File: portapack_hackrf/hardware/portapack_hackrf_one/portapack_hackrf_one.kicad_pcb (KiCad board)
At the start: 4 copper layers, 120 x 75 mm, 92 parts, among them J2 MICROSD_DETSW, J3 KINGTECH_DW0240A2BZ_FPC, P1 TRRS_SW_JACK, P2 TRS_JACK, P20 HACKRF_ONE_P20, P22 HACKRF_ONE_P22, P28 HACKRF_ONE_P28, P3 TRS_JACK, Q1 MOSFET_P, Q2 MOSFET_P, Q3 MOSFET_N, SW1 CK_TSWB-3N-CB, U1 5M40ZE64, U2 REGULATOR_SOT23_5, U3 WM8731SEDS, X1 MIC_ELECTRET

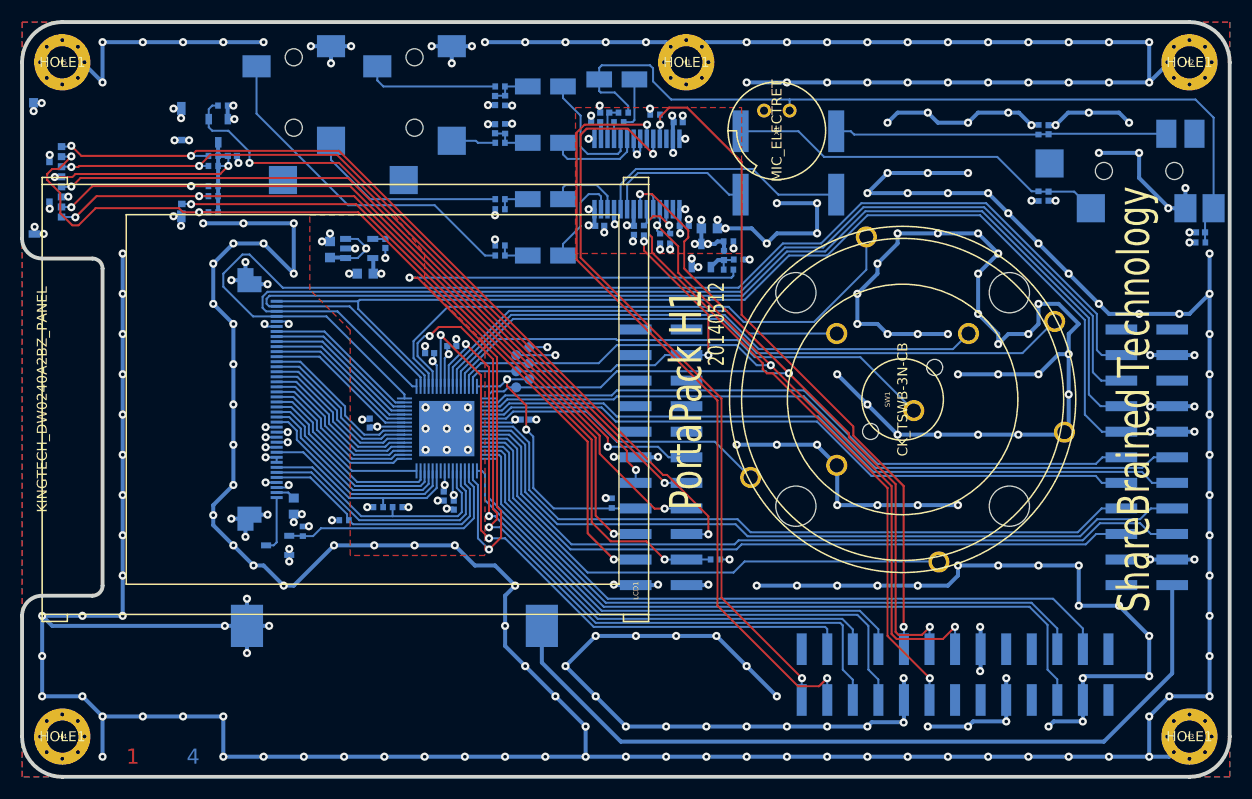
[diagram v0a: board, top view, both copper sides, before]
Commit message: Major revision 20140701 of PortaPack H1 PCB design for second prototype. Slight changes to signal mapping to CPLD. Added lots of signal integrity and EMC tweaks, including series resistor terminations and ferrites on audio jacks. Removed a bunch of unnecessary components. Shifted LCD to 1.8V I/O operation. Added more bypass capacitors.
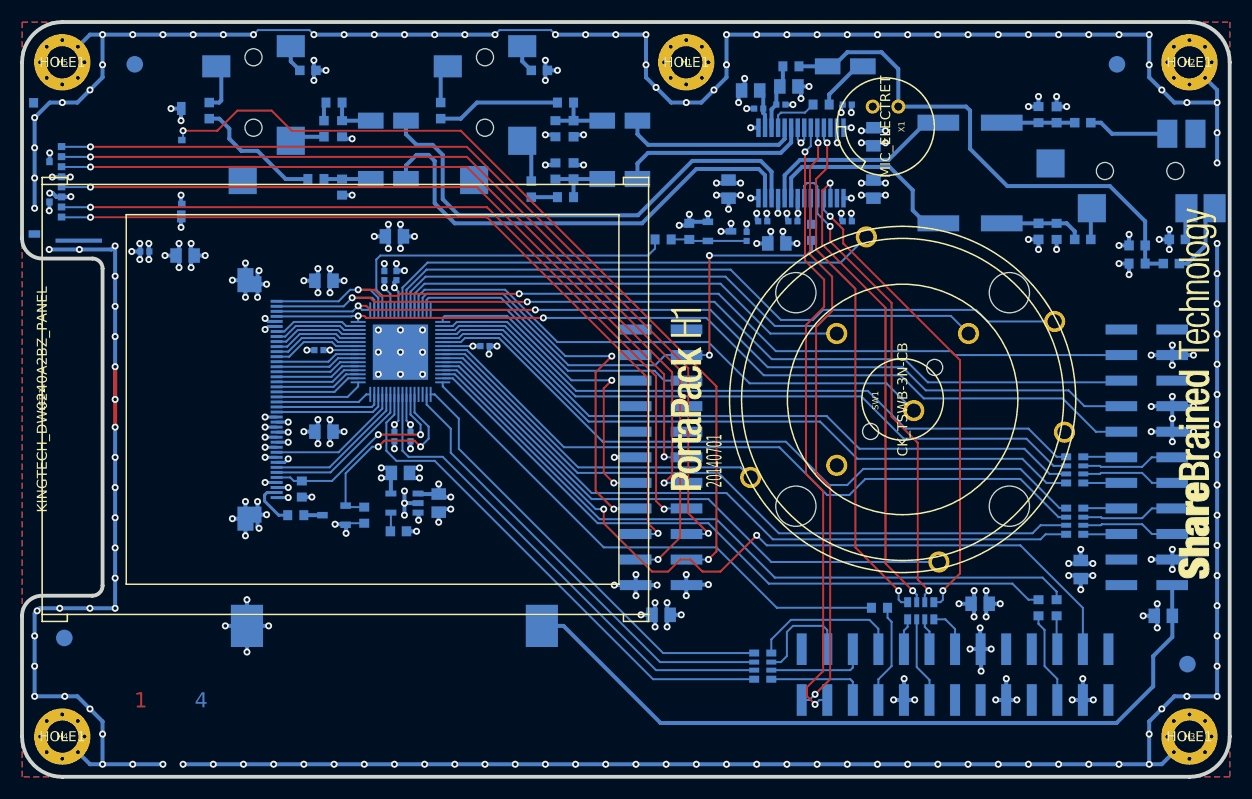
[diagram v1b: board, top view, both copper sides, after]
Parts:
- removed Q3: MOSFET_N, ipc_sot:IPC_SOT95P230X110-3N
- removed R23, R24, R25, R27, R28, R29, R31, R32, R33: 10K, ipc_resc:IPC_RESC1005X40N
- removed R26: 100R, ipc_resc:IPC_RESC1005X40N
- removed R30: R, ipc_resc:IPC_RESC1608X55N
- removed TP1, TP2, TP3, TP4, TP5, TP6: TP, tp:TP_1MM
- added C31: 100N, ipc_capc:IPC_CAPC1005X55N, B.Cu at (98.6, 141.2)
- added C32: 10U, ipc_capc:IPC_CAPC2012X140N, B.Cu at (123.5, 158.9)
- added C33: 100N, ipc_capc:IPC_CAPC1005X55N, B.Cu at (97.0, 141.2)
- added C34: 10U, ipc_capc:IPC_CAPC2012X140N, B.Cu at (97.0, 121.3)
- added C35: 100N, ipc_capc:IPC_CAPC1005X55N, B.Cu at (89.5, 132.6)
- added C36: 10U, ipc_capc:IPC_CAPC2012X140N, B.Cu at (90.0, 125.7)
- added C37: 10U, ipc_capc:IPC_CAPC2012X140N, B.Cu at (90.0, 140.7)
- added C38: 10U, ipc_capc:IPC_CAPC2012X140N, B.Cu at (101.4, 147.8)
- added C39: DNI, ipc_capc:IPC_CAPC1608X90N, B.Cu at (97.4, 150.6)
- added C40: 10U, ipc_capc:IPC_CAPC2012X140N, B.Cu at (97.6, 144.8)
- added C41: 10U, ipc_capc:IPC_CAPC2012X140N, B.Cu at (173.4, 159.0)
- added C42: 10U, ipc_capc:IPC_CAPC2012X140N, B.Cu at (155.2, 157.8)
- added C43: 10U, ipc_capc:IPC_CAPC2012X140N, B.Cu at (165.2, 154.4)
- added FID1: FIDUCIAL, fiducial:FIDUCIAL_65MIL, B.Cu at (71.2, 104.2)
- added FID2: FIDUCIAL, fiducial:FIDUCIAL_65MIL, B.Cu at (168.8, 104.2)
- added FID3: FIDUCIAL, fiducial:FIDUCIAL_65MIL, B.Cu at (64.2, 161.2)
- added FID4: FIDUCIAL, fiducial:FIDUCIAL_65MIL, B.Cu at (175.8, 163.8)
- added L1: L, ipc_indc:IPC_INDC1608X95N, B.Cu at (111.4, 104.8)
- added L10: L, ipc_indc:IPC_INDC1608X95N, B.Cu at (88.4, 104.8)
- added L2: L, ipc_indc:IPC_INDC1608X95N, B.Cu at (110.6, 116.6)
- added L3: L, ipc_indc:IPC_INDC1608X95N, B.Cu at (101.6, 108.8)
- added L4: L, ipc_indc:IPC_INDC1608X95N, B.Cu at (165.4, 121.6)
- added L5: L, ipc_indc:IPC_INDC1608X95N, B.Cu at (165.4, 110.0)
- added L6: L, ipc_indc:IPC_INDC1608X95N, B.Cu at (174.8, 121.6)
- added L7: L, ipc_indc:IPC_INDC1608X95N, B.Cu at (90.0, 110.6)
- added L8: L, ipc_indc:IPC_INDC1608X95N, B.Cu at (78.6, 108.8)
- added L9: L, ipc_indc:IPC_INDC1608X95N, B.Cu at (174.2, 124.0)
- added LOGO1: SHAREBRAINED, sharebrained:sharebrained_text_300, F.Cu at (176.7, 137.0)
- added LOGO2: PORTAPACK_H1, sharebrained:portapack_text_300, F.Cu at (126.0, 137.5)
- added RP1: 100R, ipc_resc:IPC_RESCAXS80P160X320X60-8N, B.Cu at (149.3, 158.5)
- added RP4: 100R, ipc_resc:IPC_RESCAXS80P160X320X60-8N, B.Cu at (133.6, 164.0)
- added RP6: 100R, ipc_resc:IPC_RESCAXS80P160X320X60-8N, B.Cu at (164.6, 144.5)
- added RP7: 100R, ipc_resc:IPC_RESCAXS80P160X320X60-8N, B.Cu at (164.6, 149.6)
- C1, C2: value 220U -> 100N; footprint ipc_capae:IPC_CAPAE830X620N -> ipc_capc:IPC_CAPC1005X55N
- C10, C4, C5, C6: value 220P -> 100N
- C11, C12: value 1U -> 10U; footprint ipc_capae:IPC_CAPAE430X540N -> ipc_capc:IPC_CAPC2012X140N
- C13: footprint ipc_capae:IPC_CAPAE430X540N -> ipc_capc:IPC_CAPC2012X140N
- C14: value 10U -> 220P; footprint ipc_capae:IPC_CAPAE430X540N -> ipc_capc:IPC_CAPC1608X95N
- C15, C22, C25: value 100N -> 220P; footprint ipc_capc:IPC_CAPC1005X55N -> ipc_capc:IPC_CAPC1608X95N
- C16, C24: value 100N -> 1U; footprint ipc_capc:IPC_CAPC1005X55N -> ipc_capae:IPC_CAPAE430X540N
- C17: footprint ipc_capc:IPC_CAPC1608X95N -> ipc_capae:IPC_CAPAE430X540N
- C18, C19: value 100N -> 220U; footprint ipc_capc:IPC_CAPC1005X55N -> ipc_capae:IPC_CAPAE830X620N
- C20, C21: value 100N -> 10U; footprint ipc_capc:IPC_CAPC1005X55N -> ipc_capae:IPC_CAPAE430X540N
- C23: value DNI -> 220P; footprint ipc_capc:IPC_CAPC1005X55N -> ipc_capc:IPC_CAPC1608X95N
- C26, C7: value 100N -> 10U; footprint ipc_capc:IPC_CAPC1005X55N -> ipc_capc:IPC_CAPC2012X140N
- C27: value 10U -> 100N; footprint ipc_capc:IPC_CAPC1608X95N -> ipc_capc:IPC_CAPC1005X55N
- C3: value 1U -> 100N; footprint ipc_capae:IPC_CAPAE430X540N -> ipc_capc:IPC_CAPC1005X55N
- C8: footprint ipc_capc:IPC_CAPC1608X95N -> ipc_capc:IPC_CAPC2012X140N
- C9: value 220P -> 10U; footprint ipc_capc:IPC_CAPC1005X55N -> ipc_capc:IPC_CAPC2012X140N
- P1: value TRRS_SW_JACK -> TRS_JACK; footprint cui:CUI_SJ-43516-SMT -> cui:CUI_SJ-3524-SMT
- P2: value TRS_JACK -> TRRS_SW_JACK; footprint cui:CUI_SJ-3524-SMT -> cui:CUI_SJ-43516-SMT
- R1: value R -> 100R; footprint ipc_resc:IPC_RESC1005X40N -> ipc_resc:IPC_RESC1608X55N
- R10: value 5K6 -> R; footprint ipc_resc:IPC_RESC1005X40N -> ipc_resc:IPC_RESC1608X55N
- R11: value 5K6 -> 47K; footprint ipc_resc:IPC_RESC1005X40N -> ipc_resc:IPC_RESC1608X55N
- R12, R13, R14: value 10K -> 47K; footprint ipc_resc:IPC_RESC1005X40N -> ipc_resc:IPC_RESC1608X55N
- R15, R16: value 10K -> 100R; footprint ipc_resc:IPC_RESC1005X40N -> ipc_resc:IPC_RESC1608X55N
- R17, R19, R20, R22, R7, R8: footprint ipc_resc:IPC_RESC1005X40N -> ipc_resc:IPC_RESC1608X55N
- R18: value 47K -> 680R; footprint ipc_resc:IPC_RESC1005X40N -> ipc_resc:IPC_RESC1608X55N
- R2, R3: value 47K -> 100R; footprint ipc_resc:IPC_RESC1005X40N -> ipc_resc:IPC_RESC1608X55N
- R21: value 100R -> R; footprint ipc_resc:IPC_RESC1005X40N -> ipc_resc:IPC_RESC1608X55N
- R4: value 47K -> 10K; footprint ipc_resc:IPC_RESC1005X40N -> ipc_resc:IPC_RESC1608X55N
- R5: value 680R -> 47K; footprint ipc_resc:IPC_RESC1005X40N -> ipc_resc:IPC_RESC1608X55N
- R6: value 10K -> 5K6; footprint ipc_resc:IPC_RESC1005X40N -> ipc_resc:IPC_RESC1608X55N
- R9: value 100K -> 5K6; footprint ipc_resc:IPC_RESC1005X40N -> ipc_resc:IPC_RESC1608X55N
- U1: value 5M40ZE64 -> WM8731SEDS; footprint ipc_qfp:IPC_QFP40P900X900X120-65N -> ipc_sop:IPC_SOP65P780X200-28N
- U3: value WM8731SEDS -> 5M40ZE64; footprint ipc_sop:IPC_SOP65P780X200-28N -> ipc_qfp:IPC_QFP40P900X900X120-65N
- moved P2 73.6 mm to (172.1, 114.8), turned to 180 degrees
- moved P1 73.5 mm to (106.0, 106.0), turned to 270 degrees
- moved C23 67.9 mm to (162.8, 109.2), turned to 90 degrees
- moved R1 65.0 mm to (162.8, 158.2), turned to 270 degrees
- moved R17 63.5 mm to (170.8, 124.0), turned to 180 degrees
- moved C22 59.4 mm to (161.0, 120.8), turned to 90 degrees
- moved R13 56.6 mm to (91.8, 110.6), turned to 90 degrees
- moved R11 56.3 mm to (162.8, 120.8), turned to 90 degrees
- moved C25 53.4 mm to (170.8, 122.2), turned to 180 degrees
- moved R4 53.4 mm to (123.7, 121.6)
- moved R3 50.1 mm to (145.2, 158.2), turned to 0 degrees
- moved C18 48.3 mm to (154.2, 120.0)
- moved C6 45.6 mm to (133.2, 108.6)
- moved U1 44.0 mm to (137.4, 114.0), turned to 90 degrees
- moved R2 40.9 mm to (161.0, 158.2), turned to 270 degrees
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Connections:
- net /SD_CLK renamed /hackrf_if/SD_CLK
- net /VBAT renamed /hackrf_if/VBAT
- C1 pad 1: /LHPOUT -> /audio/CODEC_VDD
- C10 pad 1: Net-(C10-Pad1) -> /audio/MICBIAS
- C11 pad 1: /LLINEIN -> /audio/CODEC_VDD
- C11 pad 2: Net-(C11-Pad2) -> GND
- C12 pad 1: /RLINEIN -> /audio/MICBIAS
- C12 pad 2: Net-(C10-Pad1) -> GND
- C13 pad 1: /LOUT -> /audio/CODEC_VDD
- C13 pad 2: Net-(C13-Pad2) -> GND
- C14 pad 1: /ROUT -> GND
- C16 pad 1: +3.3V -> /audio/LLINEIN
- C16 pad 2: GND -> Net-(C14-Pad2)
- C17 pad 1: +3.3V -> /audio/RLINEIN
- C17 pad 2: GND -> Net-(C15-Pad1)
- C18 pad 1: +3.3V -> /audio/LHPOUT
- C18 pad 2: GND -> Net-(C18-Pad2)
- C19 pad 1: /CODEC_VDD -> /audio/RHPOUT
- C19 pad 2: GND -> Net-(C19-Pad2)
- C2 pad 1: /RHPOUT -> /audio/CODEC_VDD
- C2 pad 2: Net-(C2-Pad2) -> GND
- C20 pad 1: +3.3V -> /audio/LOUT
- C20 pad 2: GND -> Net-(C20-Pad2)
- C21 pad 1: +3.3V -> /audio/ROUT
- C21 pad 2: GND -> Net-(C21-Pad2)
- C22 pad 1: +1.8V -> GND
- C22 pad 2: GND -> Net-(C18-Pad2)
- C23 pad 1: Net-(C23-Pad1) -> Net-(C19-Pad2)
- C24 pad 1: GND -> Net-(C24-Pad1)
- C24 pad 2: /CODEC_VDD -> Net-(C24-Pad2)
- C25 pad 1: /CODEC_VDD -> Net-(C24-Pad2)
- C26 pad 1: +1.8V -> +3.3V
- C27 pad 1: +1.8V -> +3.3V
- C28 pad 1: GND -> +3.3V
- C28 pad 2: /CODEC_VDD -> GND
- C29 pad 1: Net-(C29-Pad1) -> +1.8V
- C3 pad 1: Net-(C3-Pad1) -> /audio/CODEC_VDD
- C3 pad 2: Net-(C3-Pad2) -> GND
- C30 pad 1: /MICBIAS -> +3.3V
- C4 pad 1: GND -> /audio/CODEC_VDD
- C4 pad 2: Net-(C1-Pad2) -> GND
- C5 pad 1: Net-(C2-Pad2) -> /audio/CODEC_VDD
- C6 pad 1: Net-(C3-Pad2) -> /audio/VMID
- C7 pad 1: /CODEC_VDD -> /audio/CODEC_VDD
- C7 pad 2: Net-(C7-Pad2) -> GND
- C8 pad 1: /CODEC_VDD -> /audio/VMID
- C9 pad 1: GND -> /audio/CODEC_VDD
- C9 pad 2: Net-(C11-Pad2) -> GND
- J2 pad 1: /SD_DAT2 -> /hackrf_if/SD_DAT2
- J2 pad 2: /SD_DAT3 -> /hackrf_if/SD_DAT3
- J2 pad 3: /SD_CMD -> /hackrf_if/SD_CMD
- J2 pad 4: Net-(C15-Pad1) -> +3.3V
- J2 pad 7: /SD_DAT0 -> /hackrf_if/SD_DAT0
- J2 pad 8: /SD_DAT1 -> /hackrf_if/SD_DAT1
- J2 pad A: /SD_CD -> GND
- J2 pad B: GND -> /hackrf_if/SD_CD
- J3 pad 1: Net-(J3-Pad1) -> GND
- J3 pad 10: /LCD_WR# -> /hackrf_if/LCD_WR#
- J3 pad 16: /LCD_DB17 -> GND
- J3 pad 17: /LCD_DB16 -> GND
- J3 pad 18: /LCD_DB15 -> /hackrf_if/LCD_DB15
- J3 pad 19: /LCD_DB14 -> /hackrf_if/LCD_DB14
- J3 pad 20: /LCD_DB13 -> /hackrf_if/LCD_DB13
- J3 pad 21: /LCD_DB12 -> /hackrf_if/LCD_DB12
- J3 pad 22: /LCD_DB11 -> /hackrf_if/LCD_DB11
- J3 pad 23: /LCD_DB10 -> /hackrf_if/LCD_DB10
- J3 pad 24: /LCD_DB9 -> /hackrf_if/LCD_DB9
- J3 pad 25: /LCD_DB8 -> /hackrf_if/LCD_DB8
- J3 pad 26: /LCD_DB7 -> /hackrf_if/LCD_DB7
- J3 pad 27: /LCD_DB6 -> /hackrf_if/LCD_DB6
- J3 pad 28: /LCD_DB5 -> /hackrf_if/LCD_DB5
- J3 pad 29: /LCD_DB4 -> /hackrf_if/LCD_DB4
- J3 pad 30: /LCD_DB3 -> /hackrf_if/LCD_DB3
- J3 pad 31: /LCD_DB2 -> /hackrf_if/LCD_DB2
- J3 pad 32: /LCD_DB1 -> /hackrf_if/LCD_DB1
- J3 pad 33: /LCD_DB0 -> /hackrf_if/LCD_DB0
- J3 pad 34: /LCD_TE -> /hackrf_if/LCD_TE
- J3 pad 36: +3.3V -> +1.8V
- J3 pad 37: /TP_R -> /hackrf_if/TP_R
- J3 pad 38: /TP_D -> /hackrf_if/TP_D
- J3 pad 39: /TP_L -> /hackrf_if/TP_L
- J3 pad 40: /TP_U -> /hackrf_if/TP_U
- J3 pad 5: /LCD_RESET# -> /hackrf_if/LCD_RESET#
- J3 pad 6: /LCD_RS -> /hackrf_if/LCD_RS
- J3 pad 7: /LCD_RD# -> /hackrf_if/LCD_RD#
- P1 pad 1: Net-(C3-Pad2) -> Net-(L1-Pad1)
- P1 pad 2: Net-(C1-Pad2) -> Net-(L2-Pad2)
- P1 pad 3: Net-(C2-Pad2) -> Net-(L3-Pad2)
- P1 pad 4: GND -> (no net)
- P2 pad 1: GND -> Net-(L9-Pad1)
- P2 pad 2: Net-(P2-Pad2) -> Net-(L4-Pad1)
- P2 pad 3: Net-(P2-Pad3) -> Net-(L5-Pad1)
- P2 pad 4: (no net) -> Net-(L6-Pad1)
- P20 pad 10: /GPIO3_13 -> /hackrf_if/GPIO3_13
- P20 pad 11: /GPIO3_14 -> /hackrf_if/GPIO3_14
- P20 pad 12: /GPIO3_15 -> /hackrf_if/GPIO3_15
- P20 pad 14: /TP_U -> /hackrf_if/TP_R
- P20 pad 16: /TP_L -> /hackrf_if/TP_D
- P20 pad 17: Net-(P20-Pad17) -> (no net)
- P20 pad 18: /TP_D -> /hackrf_if/TP_L
- P20 pad 2: Net-(P20-Pad2) -> (no net)
- P20 pad 20: /TP_R -> /hackrf_if/TP_U
- P20 pad 21: Net-(P20-Pad21) -> (no net)
- P20 pad 22: Net-(P20-Pad22) -> (no net)
- P20 pad 4: Net-(P20-Pad4) -> (no net)
- P20 pad 5: /GPIO3_8 -> /hackrf_if/GPIO3_8
- P20 pad 6: /GPIO3_9 -> /hackrf_if/GPIO3_9
- P20 pad 7: /GPIO3_10 -> /hackrf_if/GPIO3_10
- P20 pad 8: /GPIO3_11 -> /hackrf_if/GPIO3_11
- P20 pad 9: /GPIO3_12 -> /hackrf_if/GPIO3_12
- P22 pad 1: Net-(P22-Pad1) -> (no net)
- P22 pad 12: Net-(P22-Pad12) -> (no net)
- P22 pad 13: /I2S0_TX_SDA -> /audio/I2S0_TX_SDA
- P22 pad 14: Net-(P22-Pad14) -> (no net)
- P22 pad 15: /I2S0_WS -> /audio/I2S0_WS
- P22 pad 16: /I2S0_SCK -> /audio/I2S0_SCK
- P22 pad 17: /I2S0_MCLK -> /audio/I2S0_MCLK
- P22 pad 19: /U0_RXD -> /hackrf_if/P2_1
- P22 pad 2: Net-(P22-Pad2) -> (no net)
- P22 pad 20: /U0_TXD -> /hackrf_if/P2_0
- P22 pad 21: /P2_9 -> /hackrf_if/P2_9
- P22 pad 22: /P2_13 -> /hackrf_if/P2_13
- P22 pad 23: /P2_8 -> /hackrf_if/P2_8
- P22 pad 24: /SDA -> /audio/SDA
- P22 pad 25: Net-(P22-Pad25) -> (no net)
- P22 pad 26: /SCL -> /audio/SCL
- P22 pad 3: /RESET# -> /hackrf_if/RESET#
- P22 pad 5: /P2_4 -> /hackrf_if/P2_4
- P22 pad 6: /P2_3 -> /hackrf_if/P2_3
- P22 pad 7: Net-(P22-Pad7) -> (no net)
- P22 pad 8: Net-(P22-Pad8) -> (no net)
- P22 pad 9: Net-(P22-Pad9) -> (no net)
- P28 pad 10: /SD_POW -> /hackrf_if/P1_5
- P28 pad 13: Net-(P28-Pad13) -> (no net)
- P28 pad 14: Net-(P28-Pad14) -> (no net)
- P28 pad 15: Net-(P28-Pad15) -> (no net)
- P28 pad 16: Net-(P28-Pad16) -> (no net)
- P28 pad 17: /CPLD_TCK -> /hackrf_if/CPLD_TCK
- P28 pad 18: Net-(P28-Pad18) -> (no net)
- P28 pad 19: /CPLD_TDI -> /hackrf_if/CPLD_TDI
- P28 pad 20: Net-(P28-Pad20) -> (no net)
- P28 pad 21: Net-(P28-Pad21) -> (no net)
- P28 pad 22: Net-(P28-Pad22) -> (no net)
- P28 pad 3: /SD_CD -> /hackrf_if/SD_CD
- P28 pad 4: /SD_DAT3 -> /hackrf_if/SD_DAT3
- P28 pad 5: /SD_DAT2 -> /hackrf_if/SD_DAT2
- P28 pad 6: /SD_DAT1 -> /hackrf_if/SD_DAT1
- P28 pad 7: /SD_DAT0 -> /hackrf_if/SD_DAT0
- P28 pad 8: /P1_8 -> /hackrf_if/P1_8
- P28 pad 9: /SD_CMD -> /hackrf_if/SD_CMD
- P3 pad 1: GND -> Net-(L10-Pad1)
- P3 pad 2: Net-(P3-Pad2) -> Net-(L7-Pad1)
- P3 pad 3: Net-(P3-Pad3) -> Net-(L8-Pad1)
- Q1 pad 1: Net-(C7-Pad2) -> Net-(C1-Pad2)
- Q1 pad 3: /CODEC_VDD -> /audio/CODEC_VDD
- Q2 pad 1: /SD_POW -> /hackrf_if/LCD_BACKLIGHT#
- Q2 pad 3: Net-(C15-Pad1) -> Net-(Q2-Pad3)
- R1 pad 1: Net-(C3-Pad1) -> /hackrf_if/P2_4_R
- R1 pad 2: /MICIN -> /hackrf_if/P2_4
- R10 pad 1: GND -> Net-(C24-Pad1)
- R10 pad 2: Net-(C11-Pad2) -> /audio/MICIN
- R11 pad 1: Net-(C10-Pad1) -> GND
- R11 pad 2: GND -> Net-(C18-Pad2)
- R12 pad 1: /CODEC_VDD -> Net-(C19-Pad2)
- R13 pad 1: +3.3V -> GND
- R13 pad 2: /SD_CD -> Net-(C20-Pad2)
- R14 pad 1: Net-(C15-Pad1) -> Net-(C21-Pad2)
- R14 pad 2: /SD_DAT1 -> GND
- R15 pad 1: Net-(C15-Pad1) -> Net-(L7-Pad2)
- R15 pad 2: /SD_DAT0 -> Net-(C20-Pad2)
- R16 pad 1: Net-(C15-Pad1) -> Net-(L8-Pad2)
- R16 pad 2: /SD_CMD -> Net-(C21-Pad2)
- R17 pad 1: GND -> Net-(C24-Pad2)
- R17 pad 2: Net-(C13-Pad2) -> GND
- R18 pad 1: Net-(C14-Pad2) -> /audio/MICBIAS
- R18 pad 2: GND -> Net-(C24-Pad2)
- R19 pad 1: Net-(C15-Pad1) -> /hackrf_if/LCD_RESET#
- R19 pad 2: /SD_DAT3 -> GND
- R2 pad 1: GND -> /hackrf_if/P2_3_R
- R2 pad 2: Net-(C1-Pad2) -> /hackrf_if/P2_3
- R20 pad 1: Net-(C15-Pad1) -> +3.3V
- R20 pad 2: /SD_DAT2 -> /hackrf_if/LCD_BACKLIGHT#
- R21 pad 1: Net-(P3-Pad2) -> Net-(Q2-Pad3)
- R21 pad 2: Net-(C13-Pad2) -> Net-(J3-Pad2)
- R22 pad 1: Net-(P3-Pad3) -> /hackrf_if/CPLD_TDI
- R22 pad 2: Net-(C14-Pad2) -> /audio/I2S0_RX_SDA
- R3 pad 1: Net-(C2-Pad2) -> /hackrf_if/P2_0_R
- R3 pad 2: GND -> /hackrf_if/P2_0
- R4 pad 1: Net-(C3-Pad2) -> Net-(C1-Pad2)
- R4 pad 2: GND -> /audio/CODEC_ENABLE#
- R5 pad 1: /MICBIAS -> +3.3V
- R5 pad 2: Net-(C3-Pad2) -> Net-(C1-Pad2)
- R6 pad 1: Net-(C7-Pad2) -> Net-(C14-Pad2)
- R6 pad 2: /CODEC_ENABLE# -> Net-(L2-Pad1)
- R7 pad 1: Net-(C11-Pad2) -> Net-(C15-Pad1)
- R7 pad 2: Net-(P2-Pad2) -> Net-(L3-Pad1)
- R8 pad 1: Net-(C10-Pad1) -> GND
- R8 pad 2: Net-(P2-Pad3) -> Net-(C14-Pad2)
- R9 pad 1: +3.3V -> Net-(C15-Pad1)
- R9 pad 2: Net-(C7-Pad2) -> GND
- SW1 pad A: /SW_ROT_A -> /hackrf_if/SW_ROT_A
- SW1 pad B: /SW_ROT_B -> /hackrf_if/SW_ROT_B
- SW1 pad S1: /SW_SEL -> /hackrf_if/SW_SEL
- SW1 pad S2: /SW_D -> /hackrf_if/SW_D
- SW1 pad S3: /SW_R -> /hackrf_if/SW_R
- SW1 pad S4: /SW_U -> /hackrf_if/SW_U
- SW1 pad S5: /SW_L -> /hackrf_if/SW_L
- U1 pad 1: /TP_D -> /audio/CODEC_VDD
- U1 pad 10: /SW_ROT_B -> /audio/RHPOUT
- U1 pad 11: /SW_ROT_A -> GND
- U1 pad 12: /SW_D -> /audio/LOUT
- U1 pad 13: /SW_SEL -> /audio/ROUT
- U1 pad 14: /I2S0_TX_SDA -> /audio/CODEC_VDD
- U1 pad 15: /CPLD_TDI -> GND
- U1 pad 16: /P1_8 -> /audio/VMID
- U1 pad 17: /I2S0_WS -> /audio/MICBIAS
- U1 pad 18: /GPIO3_15 -> /audio/MICIN
- U1 pad 19: /GPIO3_14 -> /audio/RLINEIN
- U1 pad 2: /TP_L -> (no net)
- U1 pad 20: /GPIO3_12 -> /audio/LLINEIN
- U1 pad 21: /GPIO3_13 -> GND
- U1 pad 22: /SW_U -> GND
- U1 pad 23: +3.3V -> /audio/SDA
- U1 pad 24: /GPIO3_11 -> /audio/SCL
- U1 pad 25: /GPIO3_10 -> /audio/I2S0_MCLK_R
- U1 pad 26: /GPIO3_8 -> (no net)
- U1 pad 27: /GPIO3_9 -> /audio/CODEC_VDD
- U1 pad 28: /SW_L -> GND
- U1 pad 3: /TP_U -> /audio/I2S0_SCK_R
- U1 pad 4: /SW_R -> /audio/I2S0_TX_SDA_R
- U1 pad 5: /P2_13 -> /audio/I2S0_WS_R
- U1 pad 6: +3.3V -> /audio/I2S0_RX_SDA
- U1 pad 7: /P2_8 -> /audio/I2S0_WS_R
- U1 pad 8: +1.8V -> /audio/CODEC_VDD
- U1 pad 9: /P2_9 -> /audio/LHPOUT
- U2 pad 4: Net-(C23-Pad1) -> Net-(C39-Pad1)
- U3 pad 1: /CODEC_VDD -> /hackrf_if/TP_D
- U3 pad 10: /RHPOUT -> /hackrf_if/SW_D
- U3 pad 11: GND -> /hackrf_if/SW_ROT_A
- U3 pad 12: /LOUT -> /hackrf_if/SW_ROT_B
- U3 pad 13: /ROUT -> /hackrf_if/SW_SEL
- U3 pad 14: /CODEC_VDD -> /hackrf_if/P1_8
- U3 pad 15: GND -> /hackrf_if/CPLD_TDI
- U3 pad 16: Net-(C29-Pad1) -> /hackrf_if/CPLD_TCK
- U3 pad 17: /MICBIAS -> /hackrf_if/P1_5
- U3 pad 18: /MICIN -> /hackrf_if/GPIO3_15_R
- U3 pad 19: /RLINEIN -> /hackrf_if/GPIO3_14_R
- U3 pad 2: Net-(U3-Pad2) -> /hackrf_if/TP_L
- U3 pad 20: /LLINEIN -> /hackrf_if/GPIO3_12_R
- U3 pad 21: GND -> /hackrf_if/GPIO3_13_R
- U3 pad 22: GND -> /hackrf_if/GPIO3_11_R
- U3 pad 23: /SDA -> +3.3V
- U3 pad 24: /SCL -> /hackrf_if/GPIO3_10_R
- U3 pad 25: /I2S0_MCLK -> /hackrf_if/SW_U
- U3 pad 26: Net-(U3-Pad26) -> /hackrf_if/GPIO3_8_R
- U3 pad 27: /CODEC_VDD -> /hackrf_if/GPIO3_9_R
- U3 pad 28: GND -> /hackrf_if/SW_L
- U3 pad 3: /I2S0_SCK -> /hackrf_if/TP_U
- U3 pad 4: /I2S0_TX_SDA -> /audio/CODEC_ENABLE#
- U3 pad 5: /I2S0_WS -> (no net)
- U3 pad 6: /I2S0_RX_SDA -> +3.3V
- U3 pad 7: /I2S0_WS -> (no net)
- U3 pad 8: /CODEC_VDD -> +1.8V
- U3 pad 9: /LHPOUT -> /hackrf_if/SW_R
- X1 pad 1: Net-(C3-Pad2) -> Net-(C24-Pad2)
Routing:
- net GND: track 1008.3 -> 621.2 mm, vias 316 -> 290
- net /TP_R: track 127.4 -> 0.00 mm
- net /TP_L: track 120.7 -> 0.00 mm
- net /TP_D: track 119.1 -> 0.00 mm
- net /TP_U: track 113.1 -> 0.00 mm
- net /I2S0_WS: track 96.6 -> 0.00 mm, vias 3 -> 0
- net /I2S0_TX_SDA: track 95.3 -> 0.00 mm, vias 3 -> 0
- net /hackrf_if/SD_DAT3: track 0.00 -> 92.2 mm, vias 0 -> 2
- net /hackrf_if/TP_L: track 0.00 -> 91.1 mm, vias 0 -> 2
- net /hackrf_if/SD_DAT2: track 0.00 -> 90.8 mm, vias 0 -> 2
- net /hackrf_if/TP_U: track 0.00 -> 90.8 mm, vias 0 -> 2
- net /hackrf_if/TP_D: track 0.00 -> 89.7 mm, vias 0 -> 2
- net /hackrf_if/TP_R: track 0.00 -> 89.3 mm, vias 0 -> 2
- net /SD_DAT3: track 87.7 -> 0.00 mm, vias 3 -> 0
- net /hackrf_if/SD_CD: track 0.00 -> 85.9 mm, vias 0 -> 2
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- added copper zone on 2_pwr, net +1.8V
- added copper zone on 2_pwr, net /audio/CODEC_VDD
- added copper zone on 2_pwr, net GND
- removed copper zone on F.Cu, net +1.8V
- removed copper zone on F.Cu, net /CODEC_VDD
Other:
- net class Default: via_dia 0.8128 -> 0.6985; via_drill 0.3556 -> 0.3429
- rule via_min_drill: 0.3556 -> 0.3429
- rule via_min_size: 0.8128 -> 0.6985
- board text added: "20140701"
- board text removed: "20140512"
- board text removed: "PortaPack H1"
- board text removed: "ShareBrained Technology"

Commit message: Update schematic PDF, netlist, component footprints, PCB from schematic changes.
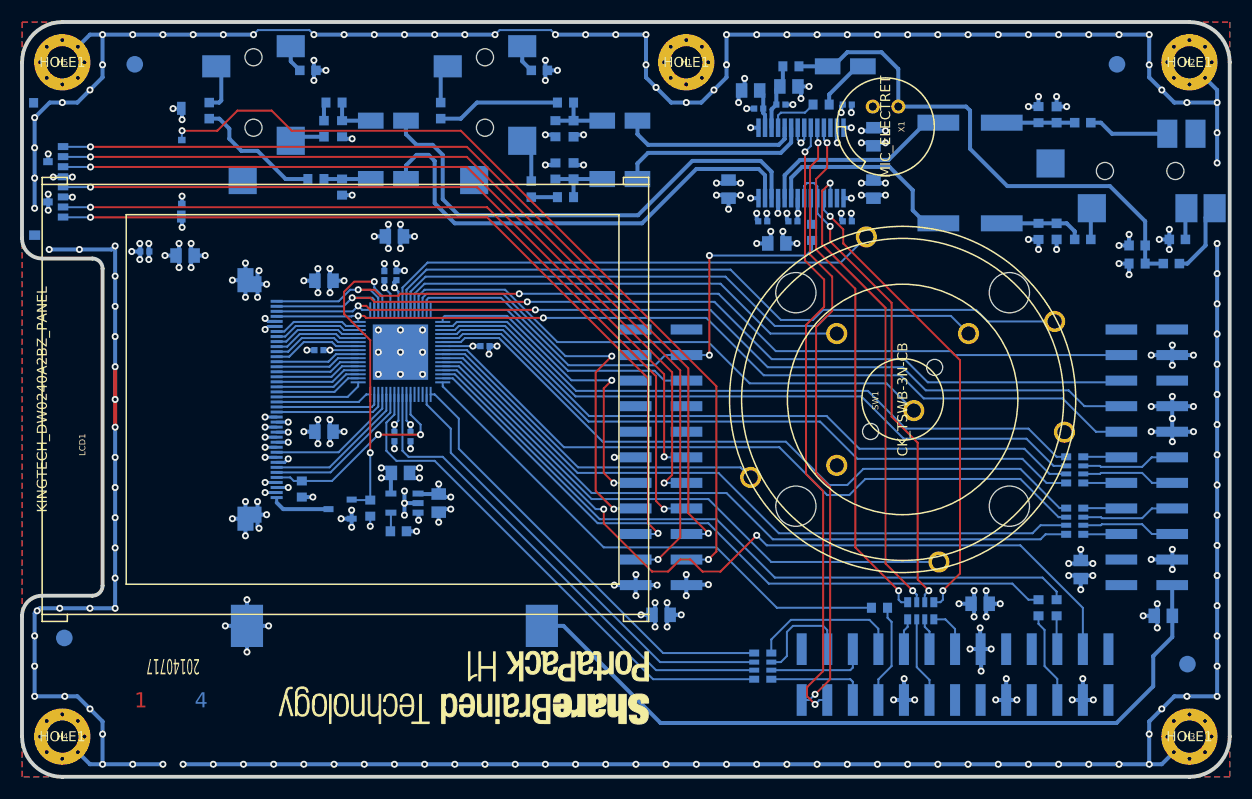
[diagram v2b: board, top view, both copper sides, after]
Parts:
- removed C1: 100N, ipc_capc:IPC_CAPC1005X55N
- removed Q2: MOSFET_P, ipc_sot:IPC_SOT95P240X110-3N
- removed R21: R, ipc_resc:IPC_RESC1608X55N
- removed R4: 10K, ipc_resc:IPC_RESC1608X55N
- removed R5: 47K, ipc_resc:IPC_RESC1608X55N
- J2: footprint alps:ALPS_SCHA4B0400 -> alps:ALPS_SCHA4B0100
- Q1: value MOSFET_P -> MOSFET_N; footprint ipc_sot:IPC_SOT95P240X110-3N -> ipc_sot:IPC_SOT95P230X110-3N
- R1, R2, R22, R3, RP1, RP4, RP6, RP7: value 100R -> 220R
- R10: value R -> 47K
- R19, R20: value 10K -> 47K
- moved LOGO1 79.0 mm to (104.0, 168.0), turned to 180 degrees
- moved Q1 46.7 mm to (91.6, 148.4), turned to 180 degrees
- moved LOGO2 29.4 mm to (113.3, 164.0), turned to 180 degrees
- moved C22 1.80 mm to (162.8, 120.8)
- moved R11 1.80 mm to (161.0, 120.8)
- moved R20 0.92 mm to (94.6, 148.3)
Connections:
- C11 pad 1: /audio/CODEC_VDD -> +3.3V
- C13 pad 1: /audio/CODEC_VDD -> +3.3V
- C2 pad 1: /audio/CODEC_VDD -> +3.3V
- C3 pad 1: /audio/CODEC_VDD -> +3.3V
- C4 pad 1: /audio/CODEC_VDD -> +3.3V
- C5 pad 1: /audio/CODEC_VDD -> +3.3V
- C7 pad 1: /audio/CODEC_VDD -> +3.3V
- C9 pad 1: /audio/CODEC_VDD -> +3.3V
- J3 pad 1: GND -> Net-(J3-Pad1)
- J3 pad 2: Net-(J3-Pad2) -> +3.3V
- Q1 pad 1: Net-(C1-Pad2) -> /hackrf_if/LCD_BACKLIGHT
- Q1 pad 2: +3.3V -> GND
- Q1 pad 3: /audio/CODEC_VDD -> Net-(J3-Pad1)
- R20 pad 1: +3.3V -> GND
- R20 pad 2: /hackrf_if/LCD_BACKLIGHT# -> /hackrf_if/LCD_BACKLIGHT
- U1 pad 1: /audio/CODEC_VDD -> +3.3V
- U1 pad 14: /audio/CODEC_VDD -> +3.3V
- U1 pad 27: /audio/CODEC_VDD -> +3.3V
- U1 pad 8: /audio/CODEC_VDD -> +3.3V
- U3 pad 37: /hackrf_if/LCD_BACKLIGHT# -> (no net)
- U3 pad 4: /audio/CODEC_ENABLE# -> /hackrf_if/LCD_BACKLIGHT
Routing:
- net /audio/CODEC_ENABLE#: track 34.3 -> 0.00 mm
- net /hackrf_if/LCD_BACKLIGHT: track 0.00 -> 30.2 mm, vias 0 -> 2
- net /audio/CODEC_VDD: track 22.0 -> 0.00 mm, vias 19 -> 0
- net /hackrf_if/LCD_BACKLIGHT#: track 20.3 -> 0.00 mm, vias 2 -> 0
- net +3.3V: track 59.4 -> 71.6 mm, vias 41 -> 53
- net Net-(C1-Pad2): track 7.56 -> 0.00 mm
- net Net-(J3-Pad1): track 0.00 -> 5.92 mm
- net Net-(J3-Pad2): track 4.78 -> 0.00 mm
- net Net-(Q2-Pad3): track 1.85 -> 0.00 mm
- net GND: track 621.2 -> 622.8 mm, vias 290 -> 293
- removed copper zone on 2_pwr, net /audio/CODEC_VDD
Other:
- board text added: "20140717"
- board text removed: "20140701"

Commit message: PCB: Footprint and trace changes to add SMT header alignment pins.
Also removed fills to keep commit/repo size down.
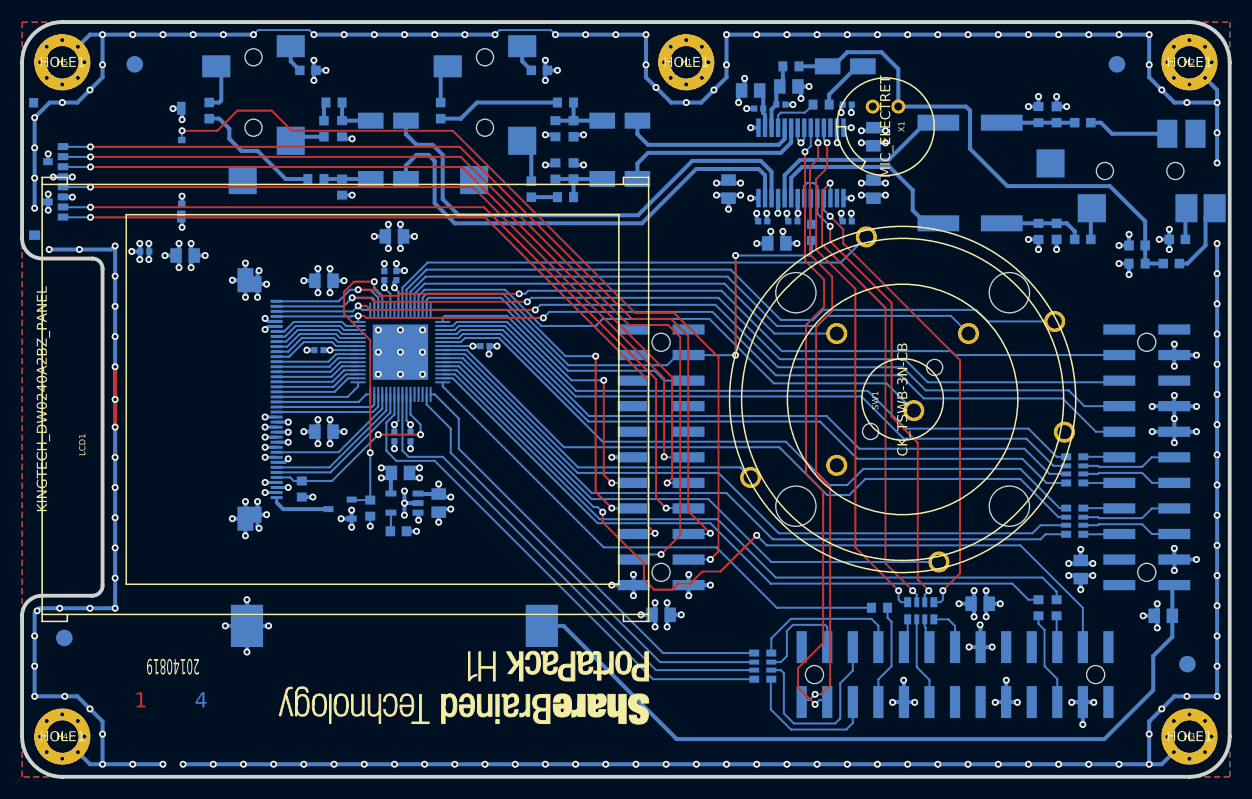
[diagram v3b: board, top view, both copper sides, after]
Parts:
- P20, P28: footprint header:HEADER_11X2_REV_SM_254 -> header:HEADER_11X2_REV_SM_254_AP
- P22: footprint header:HEADER_13X2_REV_SM_254 -> header:HEADER_13X2_REV_SM_254_AP
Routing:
- net /hackrf_if/P2_9: track 10.0 -> 19.0 mm
- net /hackrf_if/P2_13: track 10.0 -> 14.6 mm
- net /hackrf_if/SD_DAT3: track 92.1 -> 95.2 mm
- net GND: track 622.8 -> 620.1 mm, vias 293 -> 291
- net /hackrf_if/P1_8: track 41.5 -> 39.1 mm
- net /hackrf_if/SD_DAT2: track 90.7 -> 92.6 mm
- net /hackrf_if/SD_CD: track 85.9 -> 87.8 mm
- net /hackrf_if/VBAT: track 77.1 -> 78.8 mm
- net +3.3V: track 71.6 -> 69.9 mm, vias 53 -> 52
- net /hackrf_if/P1_5: track 33.1 -> 31.9 mm
- net /hackrf_if/RESET#: track 82.3 -> 83.5 mm
- net /audio/SDA: track 62.2 -> 62.9 mm
- net /hackrf_if/SW_SEL: track 55.8 -> 56.4 mm
- net /hackrf_if/SD_CMD: track 82.5 -> 82.0 mm
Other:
- board text added: "20140819"
- board text removed: "20140717"

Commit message: PCB: Segmented CPLD paste aperture.
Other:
- board text added: "20140826"
- board text removed: "20140819"
